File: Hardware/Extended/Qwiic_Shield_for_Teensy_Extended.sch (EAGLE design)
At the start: 23 parts, among them J1 QWIIC_RA, J2 QWIIC_RA, J3 QWIIC_Vertical, J4 QWIIC_Vertical, J5 ALT PWR

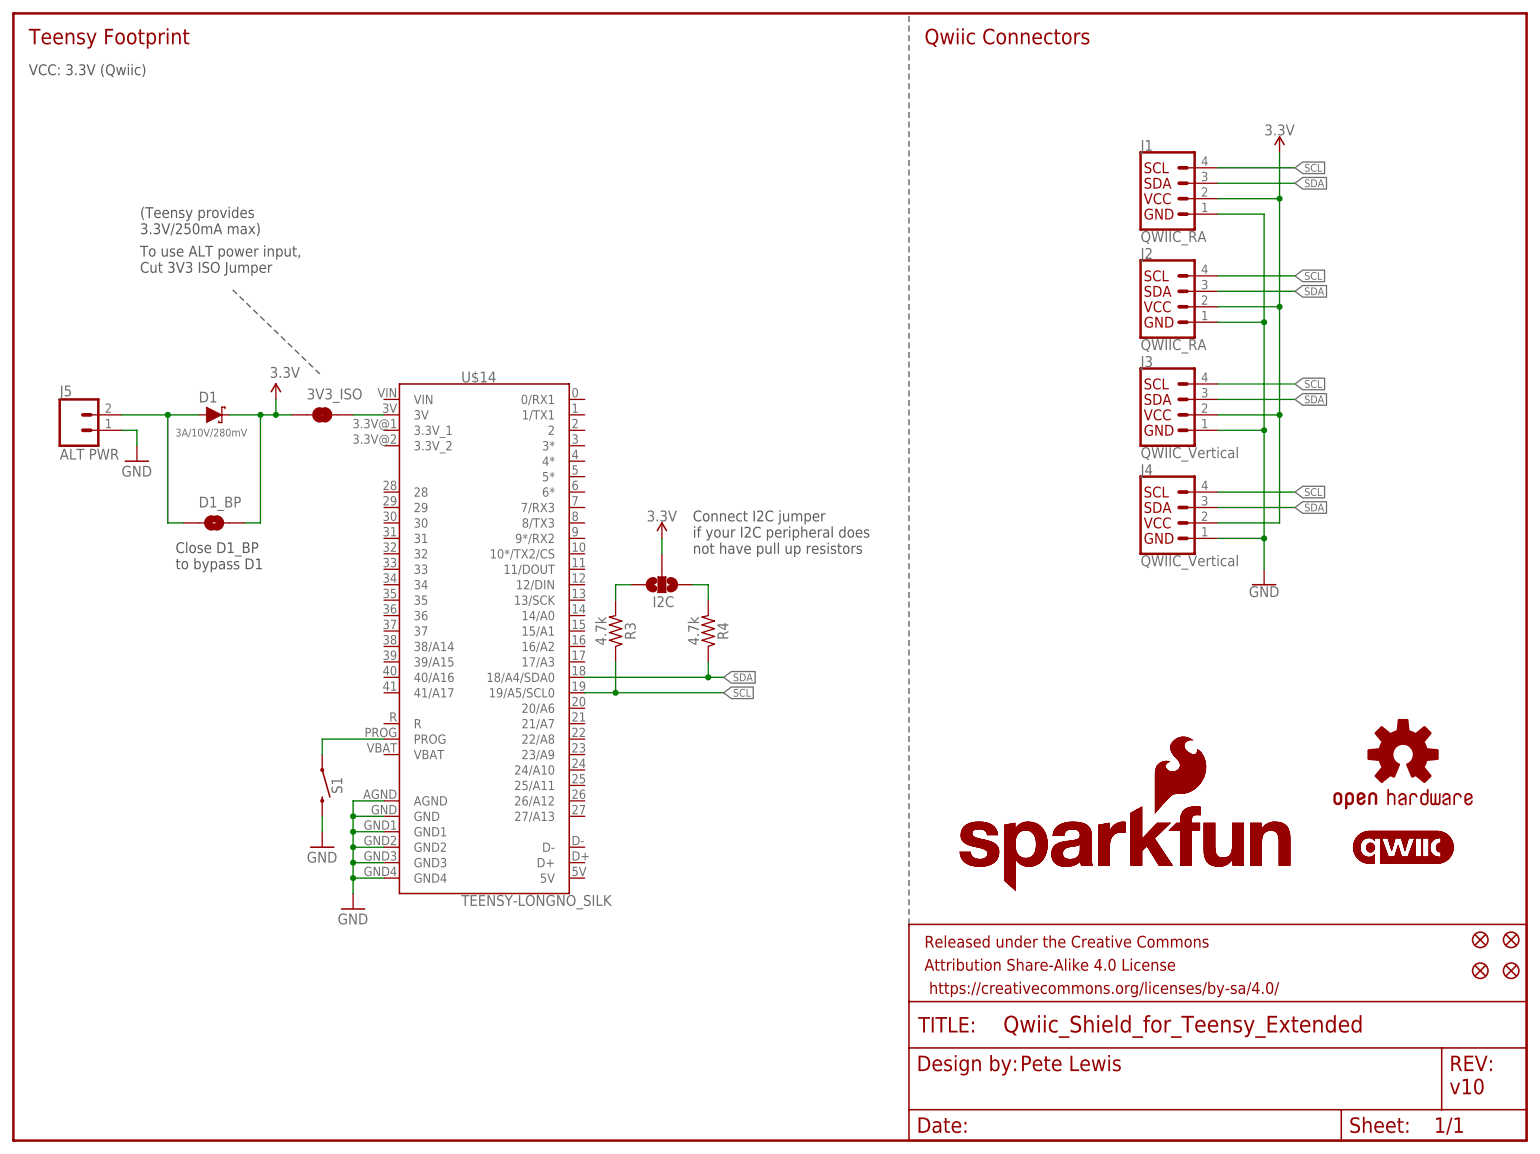
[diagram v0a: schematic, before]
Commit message: Library updates, name prefix fix, measures update
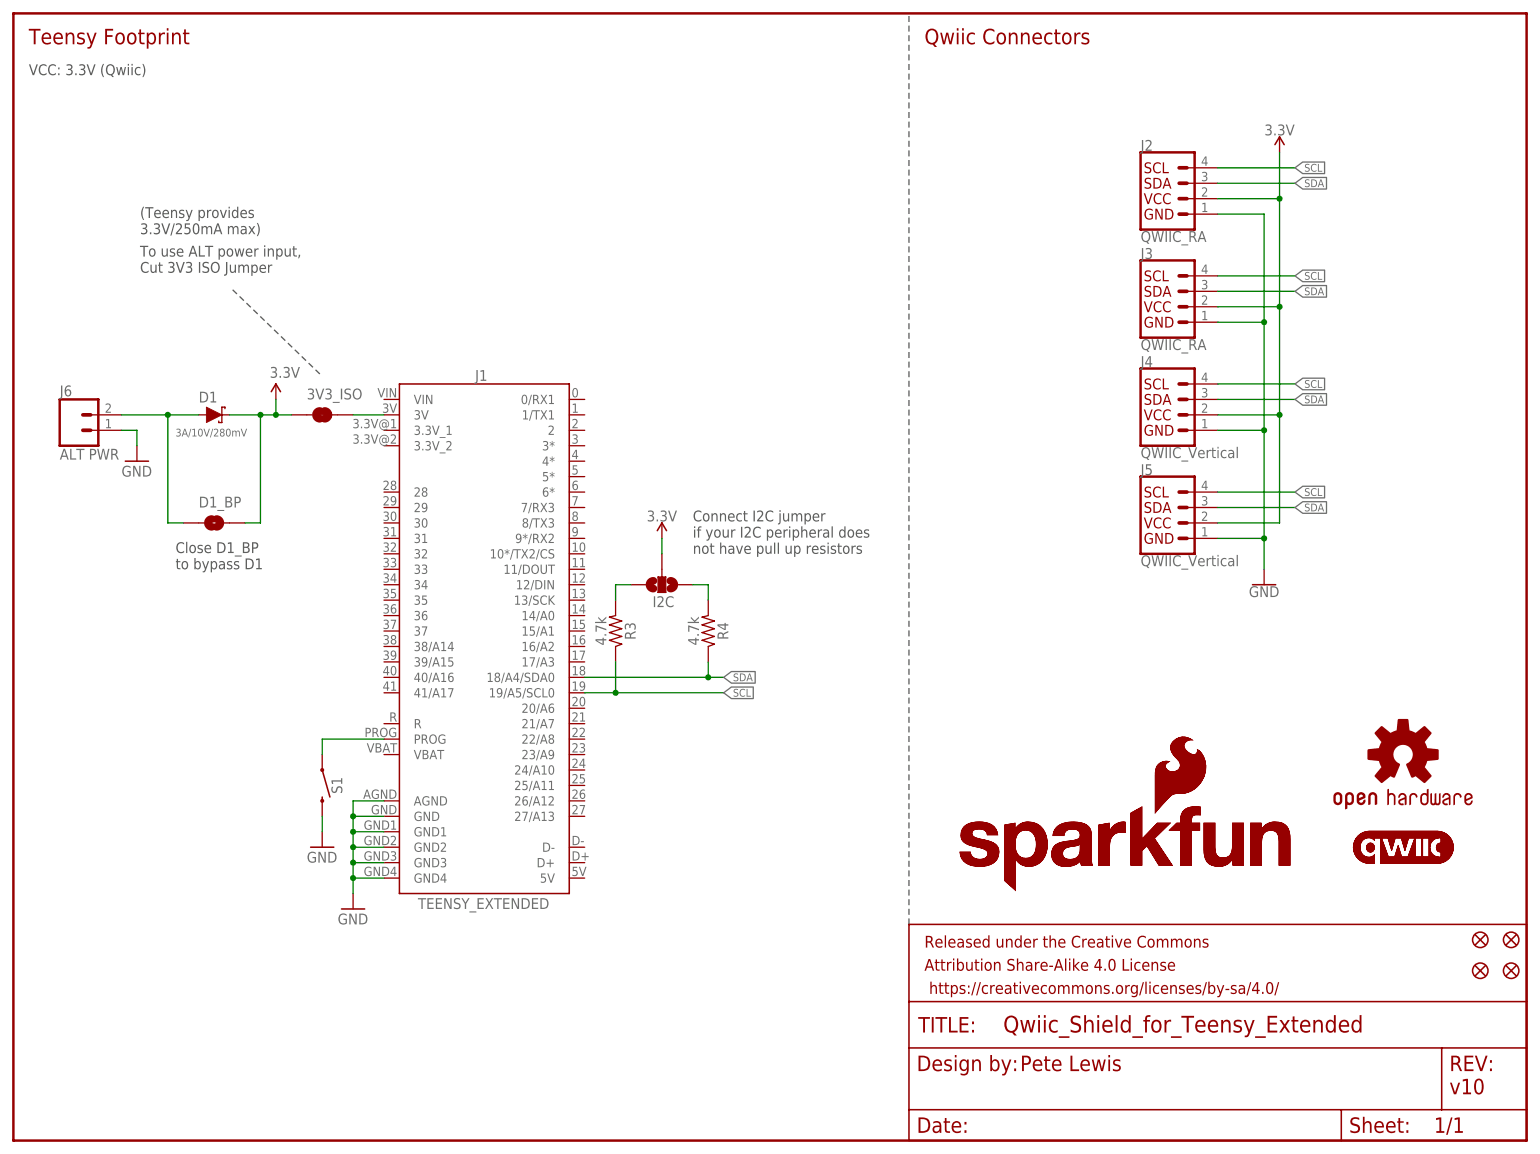
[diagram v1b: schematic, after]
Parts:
- removed U$14: TEENSY-LONGNO_SILK, teensy_boards:TEENSY-LONGNO_SILK
- added J6: ALT PWR, SparkFun-Connectors:CONN_021X02_NO_SILK
- J1: value QWIIC_RA -> TEENSY_EXTENDED; device SparkFun-Connectors:QWIIC_CONNECTORJS-1MM -> teensy_boards:TEENSY_EXTENDEDNO_SILK
- J3: value QWIIC_Vertical -> QWIIC_RA; device SparkFun-Connectors:QWIIC_CONNECTOR -> SparkFun-Connectors:QWIIC_CONNECTORJS-1MM
- J5: value ALT PWR -> QWIIC_Vertical; device SparkFun-Connectors:CONN_021X02_NO_SILK -> SparkFun-Connectors:QWIIC_CONNECTOR
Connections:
- net 3.3V: now also J5.2; no longer J1.2
- net GND: now also J1.AGND, J1.GND, J1.GND1, J1.GND2, J1.GND3, J1.GND4, J6.1; no longer J1.1, U$14.AGND, U$14.GND, U$14.GND1, U$14.GND2, U$14.GND3, U$14.GND4
- net N$3: now also J1.3V; no longer U$14.3V
- net N$4: now also J6.2; no longer J5.2
- net N$5: now also J1.PROG; no longer U$14.PROG
- net SCL: now also J1.19/A5/SCL0, J5.4; no longer J1.4, U$14.19/A5/SCL0
- net SDA: now also J1.18/A4/SDA0, J5.3; no longer J1.3, U$14.18/A4/SDA0
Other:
- moved on the sheet: J2, J3, J4
